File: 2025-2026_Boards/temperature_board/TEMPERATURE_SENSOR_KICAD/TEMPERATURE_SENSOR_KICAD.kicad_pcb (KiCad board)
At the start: 2 copper layers, 73.3 x 75.8 mm, 77 parts, among them J1 LCD Connector Pinout, J10 Conn_01x02_Pin, J11 Conn_01x02_Pin, J12 Conn_01x02_Pin, J13 Conn_01x02_Pin, J14 Conn_01x02_Pin, J15 Conn_01x02_Pin, J16 Conn_01x02_Pin, J17 Conn_01x02_Pin, J18 Conn_01x02_Pin, J19 Conn_01x02_Pin, J2 Conn_01x02_Pin, J20 Conn_01x02_Pin, J21 Conn_01x02_Pin, J22 Conn_01x02_Pin, J23 Conn_01x02_Pin, J24 Conn_01x03_Socket, J25 Conn_01x03_Socket, J3 Conn_01x02_Pin, J4 Conn_01x02_Pin, J5 Conn_01x02_Pin, J6 Conn_01x02_Pin, J7 Conn_01x02_Pin, J8 Conn_01x02_Pin, J9 Conn_01x02_Pin, U1 STM32G431CBT6, U2 TMP235A4DBZR, U3 AMS1117-3.3, U4 TCAN1057AEV-Q1, U5 TPS62932DRLR, U8 AMS1117

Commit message: Finalized board
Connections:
- J25 pad 1: CAN+ -> CAN-
- J25 pad 2: CAN- -> CAN+
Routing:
- net CAN-: track 24.2 -> 28.4 mm
- net +3.3V: track 80.4 -> 77.4 mm, vias 6 -> 5
- net CAN+: track 25.3 -> 26.8 mm
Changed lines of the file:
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@@
 			(layers "F.Cu" "F.Mask" "F.Paste")
 			(roundrect_rratio 0.25)
-			(net 49 "CAN+")
+			(net 48 "CAN-")
 			(pinfunction "Pin_1")
 			(pintype "passive")
@@
 			(layers "F.Cu" "F.Mask" "F.Paste")
 			(roundrect_rratio 0.25)
-			(net 48 "CAN-")
+			(net 49 "CAN+")
 			(pinfunction "Pin_2")
 			(pintype "passive")
@@
 	)
 	(segment
-		(start 102.25 126)
-		(end 104 127.75)
-		(width 0.2)
-		(layer "F.Cu")
-		(net 2)
-	)
-	(segment
 		(start 110 117.75)
 		(end 111.875 115.875)
@@
 	)
 	(segment
-		(start 104 127.75)
-		(end 104.5 127.75)
-		(width 0.2)
-		(layer "F.Cu")
-		(net 2)
-	)
-	(segment
 		(start 116.54 129.25)
 		(end 116.54 130.25)
@@
 		(net 2)
 	)
-	(via
-		(at 104.5 127.75)
-		(size 0.6)
-		(drill 0.3)
-		(layers "F.Cu" "B.Cu")
-		(net 2)
-	)
 	(segment
 		(start 112 116.75)
@@
 	)
 	(segment
+		(start 118.899 104.551)
+		(end 117.6 105.85)
+		(width 0.2)
+		(layer "F.Cu")
+		(net 48)
+	)
+	(segment
 		(start 118.375 109.250001)
 		(end 117.6 108.475001)
@@
 	)
 	(segment
+		(start 118.899 104.156262)
+		(end 118.899 104.551)
+		(width 0.2)
+		(layer "F.Cu")
+		(net 48)
+	)
+	(segment
+		(start 130.225 103.156802)
+		(end 129.593198 102.525)
+		(width 0.2)
+		(layer "F.Cu")
+		(net 48)
+	)
+	(segment
+		(start 119.551 103.899)
+		(end 119.156262 103.899)
+		(width 0.2)
+		(layer "F.Cu")
+		(net 48)
+	)
+	(segment
 		(start 117.771802 114.16)
 		(end 118.375 113.556802)
@@
 	)
 	(segment
-		(start 116.575 113.75)
-		(end 116.985 114.16)
+		(start 131 105.85)
+		(end 131 104.6)
 		(width 0.2)
 		(layer "F.Cu")
@@
 	)
 	(segment
-		(start 119.661647 110.025)
-		(end 119.318506 110.368141)
+		(start 120.925 102.525)
+		(end 119.551 103.899)
 		(width 0.2)
 		(layer "F.Cu")
@@
 	)
 	(segment
-		(start 129 105.85)
-		(end 129.774999 106.624999)
+		(start 129.593198 102.525)
+		(end 120.925 102.525)
+		(width 0.2)
+		(layer "F.Cu")
+		(net 48)
+	)
+	(segment
+		(start 116.575 113.75)
+		(end 116.985 114.16)
+		(width 0.2)
+		(layer "F.Cu")
+		(net 48)
+	)
+	(segment
+		(start 130.225 103.825)
+		(end 130.225 103.156802)
 		(width 0.2)
 		(layer "F.Cu")
@@
 	)
 	(segment
-		(start 118.375 113.556802)
-		(end 118.375 109.250001)
+		(start 119.156262 103.899)
+		(end 118.899 104.156262)
 		(width 0.2)
 		(layer "F.Cu")
@@
 	)
 	(segment
-		(start 129.774999 106.906803)
-		(end 126.656802 110.025)
+		(start 131 104.6)
+		(end 130.225 103.825)
 		(width 0.2)
 		(layer "F.Cu")
@@
 	)
 	(segment
-		(start 126.656802 110.025)
-		(end 119.661647 110.025)
+		(start 118.375 113.556802)
+		(end 118.375 109.250001)
 		(width 0.2)
 		(layer "F.Cu")
@@
 	)
 	(segment
-		(start 129.774999 106.624999)
-		(end 129.774999 106.906803)
+		(start 129.406802 102.975)
+		(end 121.111397 102.975)
 		(width 0.2)
 		(layer "F.Cu")
-		(net 48)
+		(net 49)
 	)
 	(segment
@@
 	)
 	(segment
-		(start 118.825 109.250001)
-		(end 119.6 108.475001)
+		(start 129 104.6)
+		(end 129.775 103.825)
 		(width 0.2)
 		(layer "F.Cu")
@@
 	)
 	(segment
-		(start 118.825 113.743198)
-		(end 118.825 109.250001)
+		(start 118.825 109.250001)
+		(end 119.6 108.475001)
 		(width 0.2)
 		(layer "F.Cu")
@@
 	)
 	(segment
-		(start 126.843198 110.475)
-		(end 119.848043 110.475)
+		(start 119.6 104.486397)
+		(end 119.6 105.85)
 		(width 0.2)
 		(layer "F.Cu")
@@
 	)
 	(segment
-		(start 130.225001 107.093197)
-		(end 126.843198 110.475)
+		(start 129.775 103.343198)
+		(end 129.406802 102.975)
 		(width 0.2)
 		(layer "F.Cu")
@@
 	)
 	(segment
-		(start 119.848043 110.475)
-		(end 119.636704 110.686339)
+		(start 118.825 113.743198)
+		(end 118.825 109.250001)
 		(width 0.2)
 		(layer "F.Cu")
@@
 	)
 	(segment
-		(start 130.225001 106.624999)
-		(end 130.225001 107.093197)
+		(start 129.775 103.825)
+		(end 129.775 103.343198)
 		(width 0.2)
 		(layer "F.Cu")
@@
 	)
 	(segment
-		(start 131 105.85)
-		(end 130.225001 106.624999)
+		(start 121.111397 102.975)
+		(end 119.6 104.486397)
+		(width 0.2)
+		(layer "F.Cu")
+		(net 49)
+	)
+	(segment
+		(start 129 105.85)
+		(end 129 104.6)
 		(width 0.2)
 		(layer "F.Cu")
@@
 			)
 		)
-	)
-	(zone
-		(net 2)
-		(net_name "+3.3V")
-		(layers "F.Cu" "B.Cu")
-		(hatch edge 0.5)
-		(connect_pads
-			(clearance 0.5)
-		)
-		(min_thickness 0.25)
-		(filled_areas_thickness no)
-		(fill yes
-			(thermal_gap 0.5)
-			(thermal_bridge_width 0.5)
-		)
-		(polygon
-			(pts
-				(xy 103.5 132.25) (xy 109.5 130.75) (xy 105.3 126.85) (xy 105 126.25) (xy 104 126.25) (xy 103.75 127.25)
-			)
-		)

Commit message: fixed can
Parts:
- moved H3 0.50 mm to (130.2, 115.0)
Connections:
- J25 pad 1: CAN- -> CAN+
- J25 pad 2: CAN+ -> CAN-
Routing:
- net CAN+: track 26.8 -> 33.1 mm
- net CAN-: track 28.4 -> 32.4 mm
- net GND: track 64.7 -> 63.9 mm
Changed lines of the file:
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@@
 	(footprint "MountingHole:MountingHole_4.3mm_M4"
 		(layer "F.Cu")
-		(at 130.25 114.5)
+		(at 130.25 115)
 		(descr "Mounting Hole 4.3mm, M4, no annular, generated by kicad-footprint-generator mountinghole.py")
 		(tags "mountinghole M4")
@@
 			(layers "F.Cu" "F.Mask" "F.Paste")
 			(roundrect_rratio 0.25)
-			(net 48 "CAN-")
+			(net 49 "CAN+")
 			(pinfunction "Pin_1")
 			(pintype "passive")
@@
 			(layers "F.Cu" "F.Mask" "F.Paste")
 			(roundrect_rratio 0.25)
-			(net 49 "CAN+")
+			(net 48 "CAN-")
 			(pinfunction "Pin_2")
 			(pintype "passive")
@@
 	)
 	(segment
-		(start 127 105.85)
-		(end 127 108.5)
-		(width 0.2)
-		(layer "F.Cu")
-		(net 1)
-	)
-	(segment
 		(start 118.5 129.25)
 		(end 119 129.75)
@@
 	)
 	(segment
-		(start 127 108.5)
-		(end 126.5 109)
-		(width 0.2)
-		(layer "F.Cu")
-		(net 1)
-	)
-	(segment
 		(start 105.08 123.5)
 		(end 105.08 123.53)
@@
 	)
 	(segment
+		(start 127 108.5)
+		(end 127 105.85)
+		(width 0.2)
+		(layer "F.Cu")
+		(net 1)
+	)
+	(segment
 		(start 108 116.75)
 		(end 108 115.75)
@@
 	)
 	(via
-		(at 126.5 109)
+		(at 127 108.5)
 		(size 0.6)
 		(drill 0.3)
@@
 	)
 	(segment
-		(start 118.899 104.551)
-		(end 117.6 105.85)
+		(start 119.406802 102.525)
+		(end 118.375 103.556802)
 		(width 0.2)
 		(layer "F.Cu")
@@
 	)
 	(segment
-		(start 116.985 114.16)
-		(end 117.771802 114.16)
+		(start 118.375 103.556802)
+		(end 118.375 103.825)
 		(width 0.2)
 		(layer "F.Cu")
@@
 	)
 	(segment
-		(start 118.899 104.156262)
-		(end 118.899 104.551)
+		(start 126.093198 109.025)
+		(end 125.225 108.156802)
 		(width 0.2)
 		(layer "F.Cu")
@@
 	)
 	(segment
-		(start 130.225 103.156802)
-		(end 129.593198 102.525)
+		(start 116.985 114.16)
+		(end 117.771802 114.16)
 		(width 0.2)
 		(layer "F.Cu")
@@
 	)
 	(segment
-		(start 119.551 103.899)
-		(end 119.156262 103.899)
+		(start 117.6 104.6)
+		(end 117.6 105.85)
 		(width 0.2)
 		(layer "F.Cu")
@@
 	)
 	(segment
-		(start 131 105.85)
-		(end 131 104.6)
+		(start 129 105.85)
+		(end 129.774999 106.624999)
 		(width 0.2)
 		(layer "F.Cu")
@@
 	)
 	(segment
-		(start 120.925 102.525)
-		(end 119.551 103.899)
+		(start 118.375 103.825)
+		(end 117.6 104.6)
 		(width 0.2)
 		(layer "F.Cu")
@@
 	)
 	(segment
-		(start 129.593198 102.525)
-		(end 120.925 102.525)
+		(start 125.225 105.406802)
+		(end 122.343198 102.525)
 		(width 0.2)
 		(layer "F.Cu")
@@
 	)
 	(segment
-		(start 130.225 103.825)
-		(end 130.225 103.156802)
+		(start 117.6 108.475001)
+		(end 117.6 105.85)
 		(width 0.2)
 		(layer "F.Cu")
@@
 	)
 	(segment
-		(start 117.6 108.475001)
-		(end 117.6 105.85)
+		(start 115.9 113.75)
+		(end 116.575 113.75)
 		(width 0.2)
 		(layer "F.Cu")
@@
 	)
 	(segment
-		(start 115.9 113.75)
-		(end 116.575 113.75)
+		(start 125.225 108.156802)
+		(end 125.225 105.406802)
 		(width 0.2)
 		(layer "F.Cu")
@@
 	)
 	(segment
-		(start 119.156262 103.899)
-		(end 118.899 104.156262)
+		(start 118.375 113.556802)
+		(end 118.375 109.250001)
 		(width 0.2)
 		(layer "F.Cu")
@@
 	)
 	(segment
-		(start 131 104.6)
-		(end 130.225 103.825)
+		(start 129.774999 107.656803)
+		(end 128.406802 109.025)
 		(width 0.2)
 		(layer "F.Cu")
@@
 	)
 	(segment
-		(start 118.375 113.556802)
-		(end 118.375 109.250001)
+		(start 128.406802 109.025)
+		(end 126.093198 109.025)
+		(width 0.2)
+		(layer "F.Cu")
+		(net 48)
+	)
+	(segment
+		(start 122.343198 102.525)
+		(end 119.406802 102.525)
 		(width 0.2)
 		(layer "F.Cu")
@@
 	)
 	(segment
-		(start 129.406802 102.975)
-		(end 121.111397 102.975)
+		(start 129.774999 106.624999)
+		(end 129.774999 107.656803)
+		(width 0.2)
+		(layer "F.Cu")
+		(net 48)
+	)
+	(segment
+		(start 124.775 108.343198)
+		(end 124.775 105.593198)
 		(width 0.2)
 		(layer "F.Cu")
@@
 	)
 	(segment
-		(start 129 104.6)
-		(end 129.775 103.825)
+		(start 128.593198 109.475)
+		(end 125.906802 109.475)
+		(width 0.2)
+		(layer "F.Cu")
+		(net 49)
+	)
+	(segment
+		(start 131 105.85)
+		(end 130.225001 106.624999)
+		(width 0.2)
+		(layer "F.Cu")
+		(net 49)
+	)
+	(segment
+		(start 125.906802 109.475)
+		(end 124.775 108.343198)
 		(width 0.2)
 		(layer "F.Cu")
@@
 	)
 	(segment
-		(start 119.6 104.486397)
-		(end 119.6 105.85)
+		(start 122.156802 102.975)
+		(end 119.593198 102.975)
+		(width 0.2)
+		(layer "F.Cu")
+		(net 49)
+	)
+	(segment
+		(start 118.825 103.825)
+		(end 119.6 104.6)
 		(width 0.2)
 		(layer "F.Cu")
@@
 	)
 	(segment
-		(start 129.775 103.343198)
-		(end 129.406802 102.975)
+		(start 118.825 103.743198)
+		(end 118.825 103.825)
 		(width 0.2)
 		(layer "F.Cu")
@@
 	)
 	(segment
-		(start 129.775 103.825)
-		(end 129.775 103.343198)
+		(start 124.775 105.593198)
+		(end 122.156802 102.975)
 		(width 0.2)
 		(layer "F.Cu")
@@
 	)
 	(segment
-		(start 117.958198 114.61)
-		(end 118.825 113.743198)
+		(start 130.225001 106.624999)
+		(end 130.225001 107.843197)
 		(width 0.2)
 		(layer "F.Cu")
@@
 	)
 	(segment
-		(start 116.575 115.02)
-		(end 116.985 114.61)
+		(start 119.593198 102.975)
+		(end 118.825 103.743198)
 		(width 0.2)
 		(layer "F.Cu")
@@
 	)
 	(segment
-		(start 121.111397 102.975)
-		(end 119.6 104.486397)
+		(start 130.225001 107.843197)
+		(end 128.593198 109.475)
 		(width 0.2)
 		(layer "F.Cu")
@@
 	)
 	(segment
-		(start 129 105.85)
-		(end 129 104.6)
+		(start 117.958198 114.61)
+		(end 118.825 113.743198)
+		(width 0.2)
+		(layer "F.Cu")
+		(net 49)
+	)
+	(segment
+		(start 116.575 115.02)
+		(end 116.985 114.61)
+		(width 0.2)
+		(layer "F.Cu")
+		(net 49)
+	)
+	(segment
+		(start 119.6 104.6)
+		(end 119.6 105.85)
 		(width 0.2)
 		(layer "F.Cu")

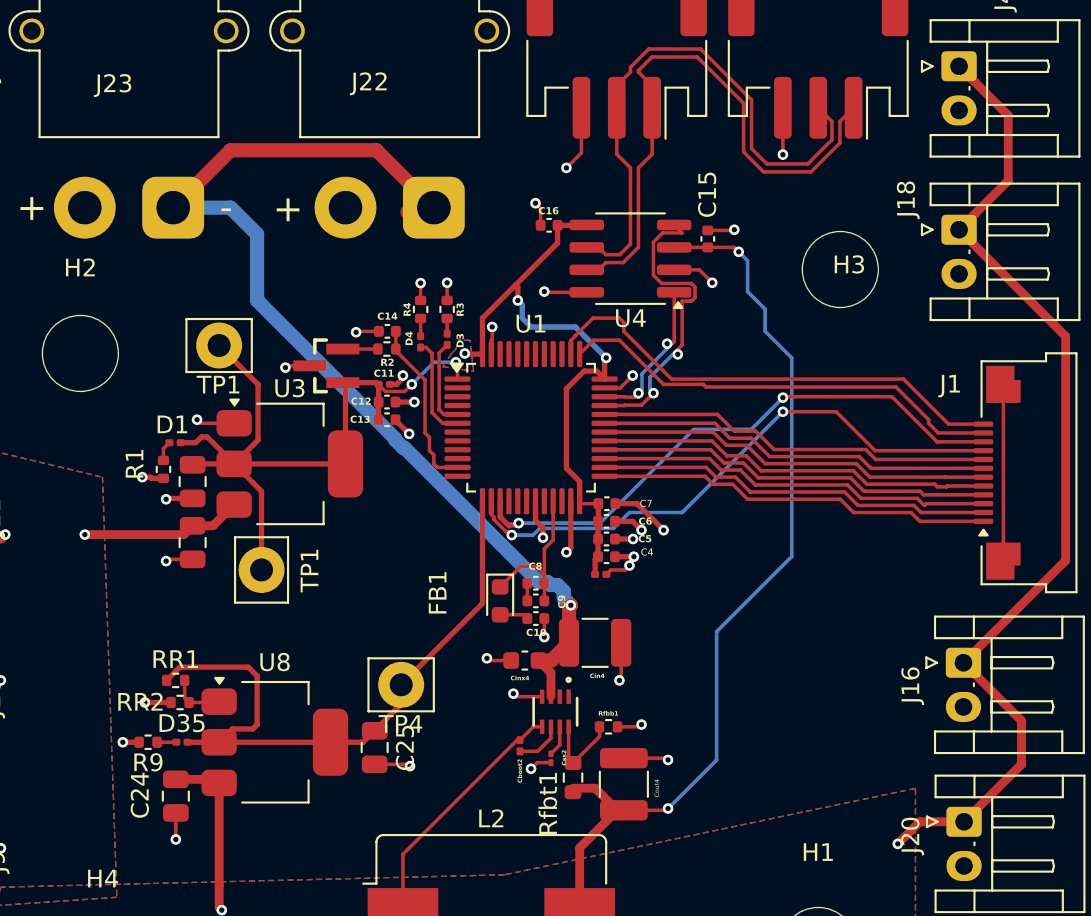
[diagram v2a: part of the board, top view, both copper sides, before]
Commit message: fixed differential pair and made new lcd wiring
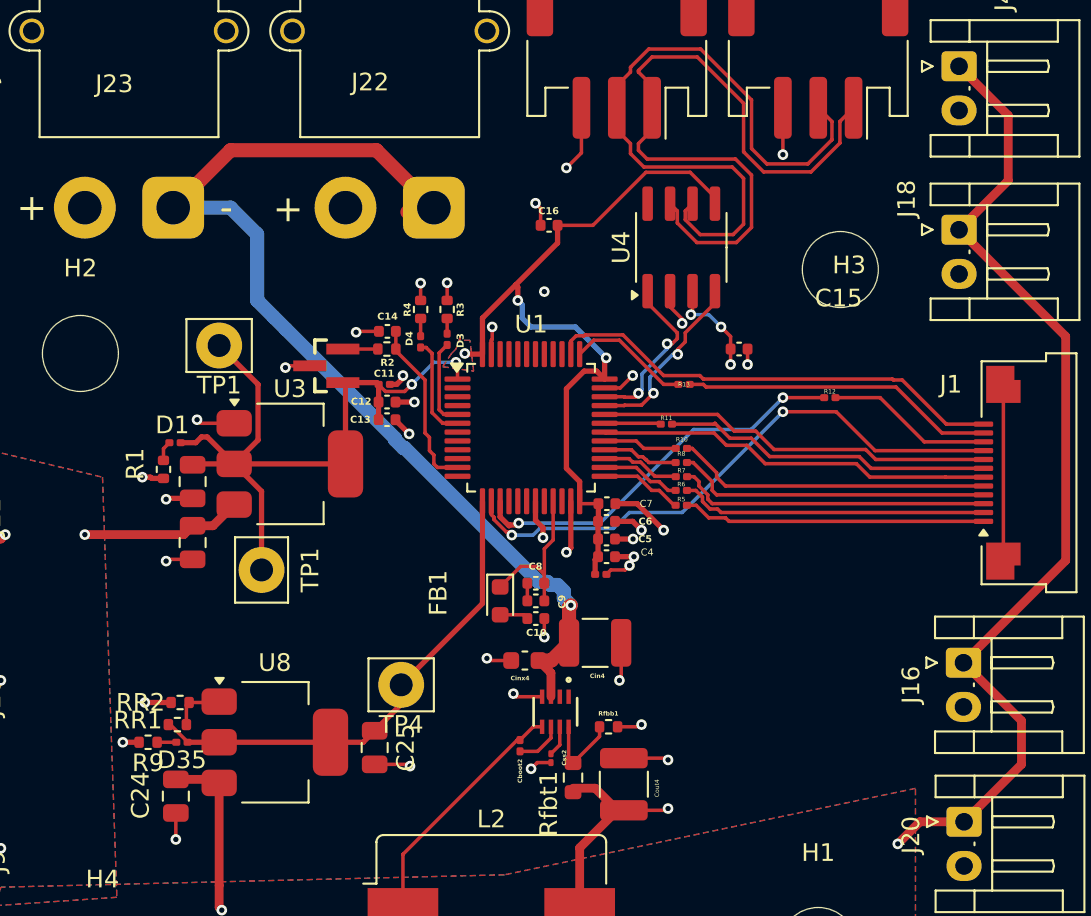
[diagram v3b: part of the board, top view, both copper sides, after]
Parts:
- added R10: 100, Resistor_SMD:R_0201_0603Metric, F.Cu at (121.3, 125.1)
- added R11: 100, Resistor_SMD:R_0201_0603Metric, F.Cu at (120.4, 123.8)
- added R12: 100, Resistor_SMD:R_0201_0603Metric, F.Cu at (129.7, 122.2)
- added R13: 100, Resistor_SMD:R_0201_0603Metric, F.Cu at (121.4, 121.5)
- added R5: 100, Resistor_SMD:R_0201_0603Metric, F.Cu at (121.2, 128.3)
- added R6: 100, Resistor_SMD:R_0201_0603Metric, F.Cu at (121.2, 127.5)
- added R7: 100, Resistor_SMD:R_0201_0603Metric, F.Cu at (121.3, 126.7)
- added R8: 100, Resistor_SMD:R_0201_0603Metric, F.Cu at (121.3, 125.9)
- moved C15 6.48 mm to (124.5, 119.5), turned to 0 degrees
- moved U4 2.94 mm to (121.2, 113.8), turned to 90 degrees
- moved RR1 2.50 mm to (92.7, 140.8)
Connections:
- U1 pad 15: Net-(J1-Pin_10) -> Net-(U1-PA7)
- U1 pad 25: Net-(J1-Pin_1) -> Net-(U1-PB11)
- U1 pad 26: Net-(J1-Pin_2) -> Net-(U1-PB12)
- U1 pad 27: Net-(J1-Pin_3) -> Net-(U1-PB13)
- U1 pad 28: Net-(J1-Pin_4) -> Net-(U1-PB14)
- U1 pad 29: Net-(J1-Pin_5) -> Net-(U1-PB15)
- U1 pad 31: Net-(J1-Pin_7) -> Net-(U1-PA9)
- U1 pad 37: Net-(J1-Pin_11) -> Net-(U1-PA13)
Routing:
- net 5V: track 237.0 -> 203.4 mm, vias 19 -> 21
- net Net-(J1-Pin_10): track 32.5 -> 9.41 mm, vias 2 -> 0
- net Net-(U1-PA7): track 0.00 -> 22.5 mm, vias 0 -> 2
- net +3.3V: track 77.4 -> 86.8 mm
- net +2.2V: track 37.3 -> 27.9 mm
- net Net-(J1-Pin_11): track 25.5 -> 17.8 mm
- net CAN+: track 33.1 -> 40.4 mm
- net FDCAN_-: track 17.7 -> 10.6 mm
- net Net-(U1-PA13): track 0.00 -> 6.95 mm
- net CAN-: track 32.4 -> 38.9 mm
- net Net-(J1-Pin_1): track 22.5 -> 17.2 mm
- net Net-(J1-Pin_2): track 22.5 -> 17.4 mm
- net Net-(J1-Pin_3): track 22.6 -> 17.7 mm
- net Net-(J1-Pin_5): track 22.5 -> 17.8 mm
- net Net-(U1-PB11): track 0.00 -> 4.70 mm
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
